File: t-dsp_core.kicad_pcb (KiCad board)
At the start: 4 copper layers, 100 x 61 mm, 164 parts, among them IC1 Logic Level Shifter - 74HCT2G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, J1 J_PWR, J10 J_DMX, J11 J_LED, J12 J_ETH, J13 u.FL DNP (IDC767 ext-antenna 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, J2 J_TDM, J3 J_T, J4 J_USBH, J5 J_MIDI, J6 J_SPDIF, J7 J_AUX, J8 J_S3, T108 Tab, T109 Tab, T110 Tab, T111 Tab, U1 Teensy 4.1 - DEVKIT, U11 Dual Buffer - SN74LVC2G125DCTR, U13 ESP32-S3-WROOM-1-N16R8, U15 LT3045EMSE#TRPBF, U16 THVD1450DR, U17 ISO7762DW, U18 TEA1-0505HI, U19 SRC4382IPFBR, U20 TLV75718PDRVR, U21 74LVC157APW, U22 IDC777-1, U23 74LVC157APW, U24 AP63203WU, U3 Power Mux & Protect - TPS2116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, U4 Optoisolators - H11L1SM - 6-S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, U5 Dual Buffer - SN74LVC2G125DCTR, U6 Dual Buffer - SN74LVC2G125DCTR, U7 Dual Buffer - SN74LVC2G125DCTR, U8 Dual Buffer - SN74LVC2G125DCTR, U9 Dual Buffer - 74HCT2G17GW,125, Y1 24.576MHz

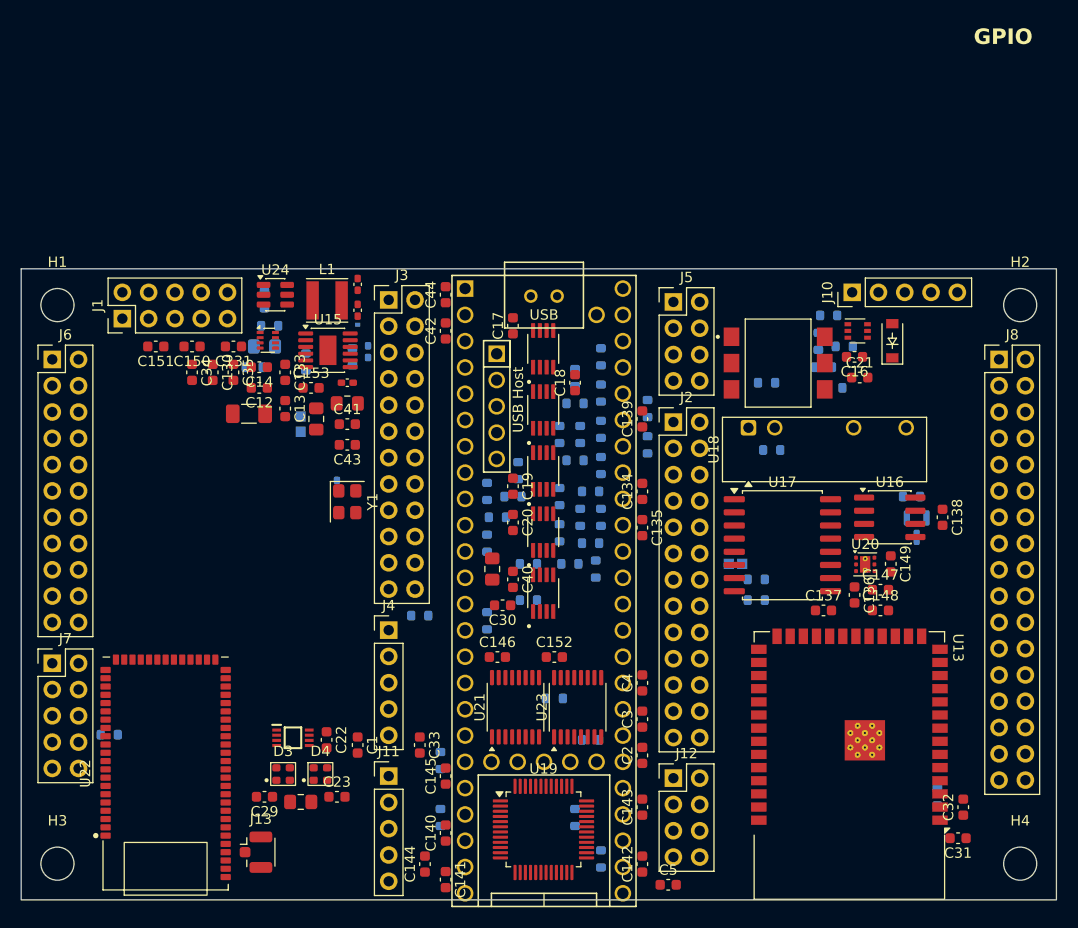
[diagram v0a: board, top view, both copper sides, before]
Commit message: Spin 2 stage 10r (board): U5 -> TSSOP-20 octal buffer at the top of the column under the Teensy, U6-U8 and C18-C20 removed, JP1 and R74 added on the back; pad nets, values and fields synced from the schematic with pcbnew; passives re-placed
Co-Authored-By: Claude Fable 5.1 <noreply@anthropic.com>
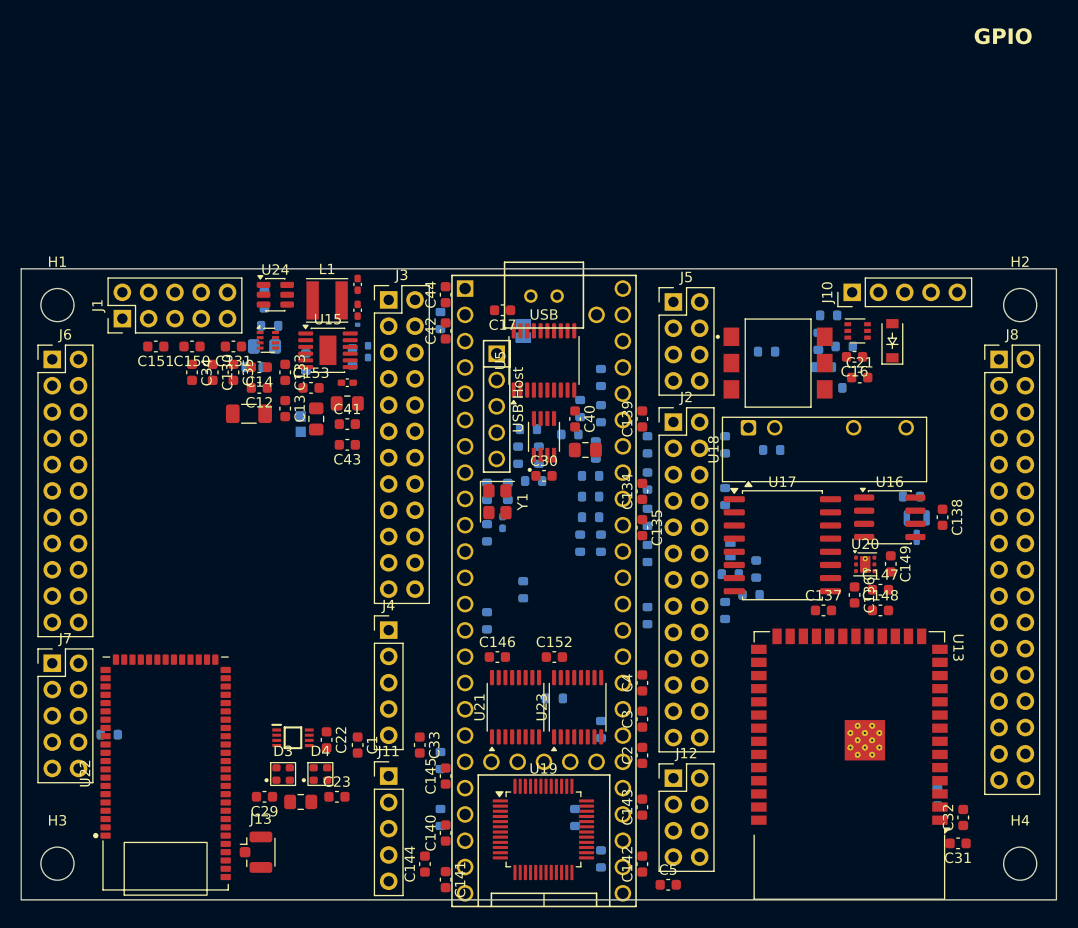
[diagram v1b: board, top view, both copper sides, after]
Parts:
- removed C18, C19, C20: 0.1 uF, Capacitor_SMD:C_0603_1608Metric
- removed U6, U7, U8: Dual Buffer - SN74LVC2G125DCTR, project_fp:SOP65P400X130-8N
- added JP1: SJ bridged, Jumper:SolderJumper-2_P1.3mm_Bridged_Pad1.0x1.5mm, B.Cu at (148.5, 145.0)
- added R74: 10k, Resistor_SMD:R_0603_1608Metric, B.Cu at (140.5, 144.0)
- U5: value Dual Buffer - SN74LVC2G125DCTR -> SN74LVC541APWR; footprint project_fp:SOP65P400X130-8N -> Package_SO:TSSOP-20_4.4x6.5mm_P0.65mm
- moved R43 21.5 mm to (168.5, 168.5), turned to 180 degrees
- moved R42 18.4 mm to (160.5, 166.5), turned to 90 degrees
- moved C40 16.6 mm to (153.5, 153.5)
- moved R60 16.4 mm to (146.5, 163.5), turned to -90 degrees
- moved R45 16.0 mm to (168.0, 161.0)
- moved U11 15.1 mm to (150.5, 155.3)
- moved C27 14.6 mm to (154.5, 156.5), turned to 0 degrees
- moved Y1 14.5 mm to (146.0, 161.5)
- moved R40 14.0 mm to (168.0, 156.0)
- moved C30 13.1 mm to (150.5, 159.0), turned to 0 degrees
- moved R47 13.1 mm to (168.0, 172.0), turned to 90 degrees
- moved R56 11.5 mm to (149.5, 159.5)
- moved R55 10.5 mm to (150.0, 157.0), turned to -90 degrees
- moved R61 10.3 mm to (148.5, 170.0), turned to -90 degrees
- moved R41 10.3 mm to (160.5, 159.5), turned to 90 degrees
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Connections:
- R40 pad 1: Net-(U6-2Y) -> /TDM2_MCLK_B
- R41 pad 1: Net-(U6-1Y) -> /TDM1_MCLK_B
- R42 pad 1: Net-(U5-1Y) -> /TDM1_LRCK_B
- R43 pad 1: Net-(U5-2Y) -> /TDM2_LRCK_B
- R44 pad 1: Net-(U7-1Y) -> /TDM1_BCLK_B
- R45 pad 1: Net-(U7-2Y) -> /TDM2_BCLK_B
- R46 pad 1: Net-(U8-1Y) -> /TDM1_DOUT_B
- R47 pad 1: Net-(U8-2Y) -> /TDM2_DOUT_B
- U5 pad 3: Net-(U5-2Y) -> MCLK1
- U5 pad 4: GND -> BCLK1
- U5 pad 5: LRCK1 -> 7_OUT1A
- U5 pad 6: Net-(U5-1Y) -> LRCK1
- U5 pad 7: GND -> MCLK1
- U5 pad 8: 3.3V -> BCLK1

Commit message: Spin 2 stage 10s: S3 and IDC777 swapped (S3 bottom-left with J8 on the left edge, IDC777 bottom-right with J6/J7 on the right edge), chips spread with 2-3 mm air, passive spacing margin 0.35 mm; change map 11.6
Co-Authored-By: Claude Fable 5.1 <noreply@anthropic.com>
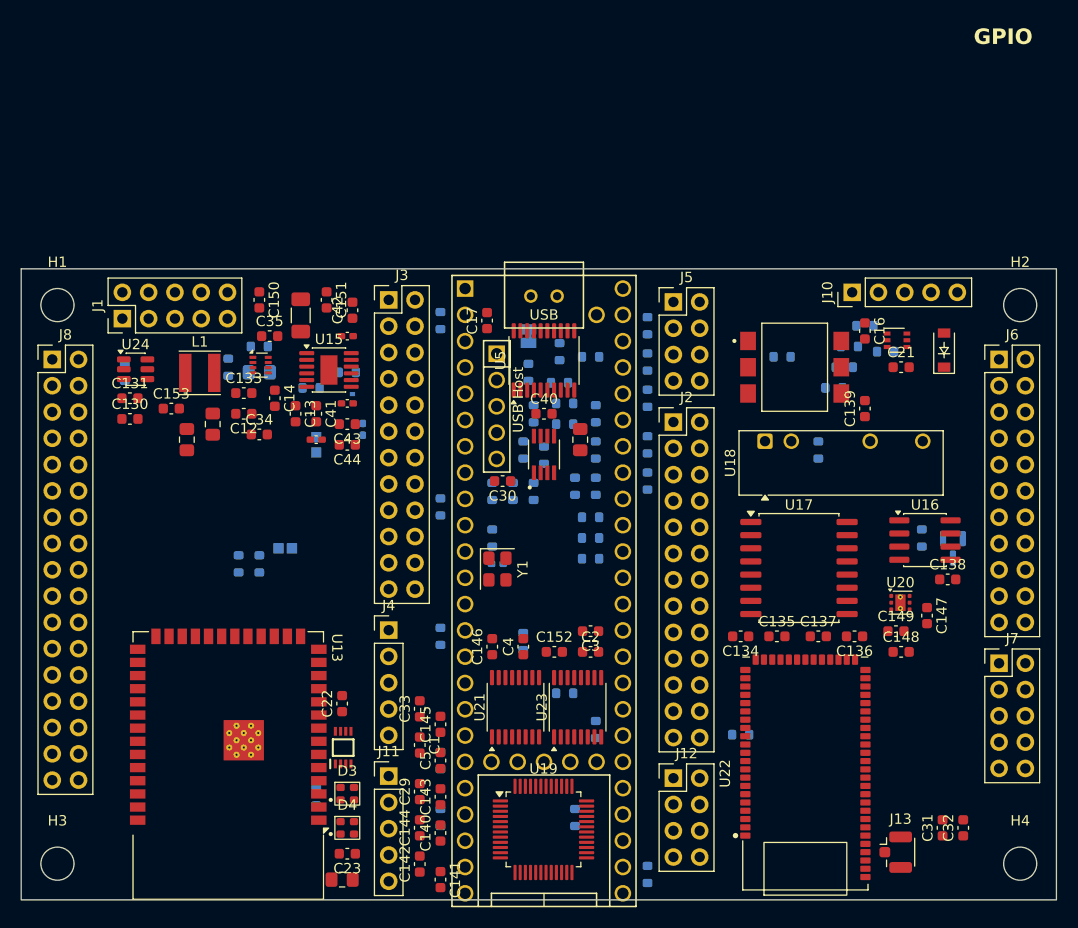
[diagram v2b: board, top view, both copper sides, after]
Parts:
- moved J6 91.5 mm to (194.5, 147.8)
- moved J7 91.5 mm to (194.5, 177.1)
- moved J8 91.5 mm to (103.0, 147.8)
- moved U22 61.8 mm to (175.8, 187.8)
- moved J13 61.8 mm to (184.9, 195.4)
- moved R72 61.0 mm to (169.5, 184.0), turned to 180 degrees
- moved R73 60.0 mm to (128.5, 190.0)
- moved U13 60.0 mm to (120.0, 187.0)
- moved R68 49.6 mm to (121.0, 167.5), turned to -90 degrees
- moved R67 48.0 mm to (123.0, 167.5)
- moved PU_EN1 43.0 mm to (125.5, 166.0), turned to 180 degrees
- moved C5 25.1 mm to (140.5, 186.5), turned to 90 degrees
- moved R43 23.0 mm to (152.5, 152.0), turned to 0 degrees
- moved R47 21.8 mm to (160.5, 151.5), turned to -90 degrees
- moved C139 21.5 mm to (181.5, 152.5)
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
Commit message: Spin 2 stage 10t: IDC777 5.4 mm further right (45.6 mm from the S3), J8 lowered beside the S3, J4 USB host header beside the Teensy host pads; passives re-placed
Co-Authored-By: Claude Fable 5.1 <noreply@anthropic.com>
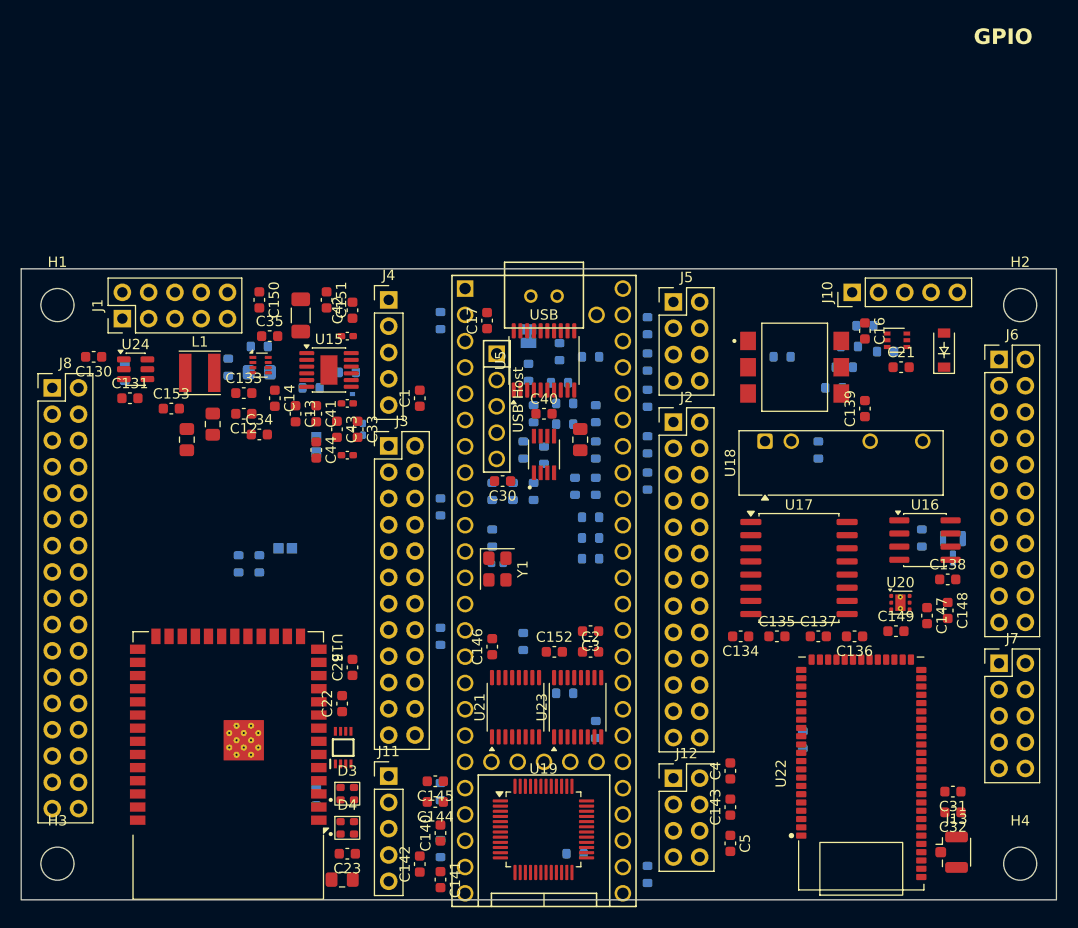
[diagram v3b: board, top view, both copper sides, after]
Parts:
- moved C1 33.5 mm to (138.5, 151.5), turned to 90 degrees
- moved J4 31.9 mm to (135.5, 142.0)
- moved C5 29.1 mm to (168.5, 194.5), turned to -90 degrees
- moved C143 28.0 mm to (168.5, 191.0)
- moved C33 27.7 mm to (132.5, 154.5), turned to -90 degrees
- moved C4 23.3 mm to (168.5, 187.5)
- moved J3 14.1 mm to (135.5, 156.1)
- moved C29 13.6 mm to (132.0, 177.5)
- moved C130 6.95 mm to (107.0, 147.5), turned to 180 degrees
- moved C148 6.02 mm to (189.5, 172.0), turned to -90 degrees
- moved R72 6.02 mm to (175.5, 184.5), turned to -90 degrees
- moved C145 5.52 mm to (140.0, 188.5), turned to 180 degrees
- moved J13 5.40 mm to (190.3, 195.4)
- moved U22 5.40 mm to (181.2, 187.8)
- moved C31 3.64 mm to (190.0, 189.5), turned to 180 degrees
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
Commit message: Spin 2 stage 10u (board): 20 terminations on 0402 footprints, values/fields/nets synced with pcbnew, passives re-placed
Co-Authored-By: Claude Fable 5.1 <noreply@anthropic.com>
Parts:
- R1, R10, R2, R3, R4, R40, R41, R42, R43, R44, R45, R46, R47, R5, R52, R55, R56, R6, R7, R9: value 49.9 ohm -> 33 ohm
- moved C31 0.50 mm to (190.5, 189.5)
- moved C32 0.50 mm to (190.5, 191.5)
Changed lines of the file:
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@@
 	(footprint "Capacitor_SMD:C_0603_1608Metric"
 		(layer "F.Cu")
-		(at 190 189.54 180)
+		(at 190.5 189.54 180)
 		(descr "Capacitor SMD 0603 (1608 Metric), square (rectangular) end terminal, IPC-7351 nominal, (Body size source: IPC-SM-782 page 76, https://www.pcb-3d.com/wordpress/wp-content/uploads/ipc-sm-782a_amendment_1_and_2.pdf)")
 		(tags "capacitor")
@@
 	(footprint "Capacitor_SMD:C_0603_1608Metric"
 		(layer "F.Cu")
-		(at 190 191.54 180)
+		(at 190.5 191.54 180)
 		(descr "Capacitor SMD 0603 (1608 Metric), square (rectangular) end terminal, IPC-7351 nominal, (Body size source: IPC-SM-782 page 76, https://www.pcb-3d.com/wordpress/wp-content/uploads/ipc-sm-782a_amendment_1_and_2.pdf)")
 		(tags "capacitor")
@@
 			)
 		)
-		(property "Value" "49.9 ohm"
+		(property "Value" "33 ohm"
 			(at 0 -1.43 90)
 			(layer "B.Fab")
@@
 			)
 		)
-		(property "LCSC" "C23185"
+		(property "LCSC" "C25105"
 			(at 0 0 0)
 			(layer "B.SilkS")
@@
 			)
 		)
-		(property "LCSC_MPN" "0603WAF499JT5E"
+		(property "LCSC_MPN" "0402WGF330JTCE"
 			(at 0 0 0)
 			(layer "B.SilkS")
@@
 			)
 		)
-		(property "Value" "49.9 ohm"
+		(property "Value" "33 ohm"
 			(at 0 -1.43 180)
 			(layer "B.Fab")
@@
 			)
 		)
-		(property "LCSC" "C23185"
+		(property "LCSC" "C25105"
 			(at 0 0 0)
 			(layer "B.SilkS")
@@
 			)
 		)
-		(property "LCSC_MPN" "0603WAF499JT5E"
+		(property "LCSC_MPN" "0402WGF330JTCE"
 			(at 0 0 0)
 			(layer "B.SilkS")
@@
 			)
 		)
-		(property "Value" "49.9 ohm"
+		(property "Value" "33 ohm"
 			(at 0 -1.43 90)
 			(layer "B.Fab")
@@
 			)
 		)
-		(property "LCSC" "C23185"
+		(property "LCSC" "C25105"
 			(at 0 0 270)
 			(layer "B.SilkS")
@@
 			)
 		)
-		(property "LCSC_MPN" "0603WAF499JT5E"
+		(property "LCSC_MPN" "0402WGF330JTCE"
 			(at 0 0 270)
 			(layer "B.SilkS")
@@
 			)
 		)
-		(property "Value" "49.9 ohm"
+		(property "Value" "33 ohm"
 			(at 0 -1.43 90)
 			(layer "B.Fab")
@@
 			)
 		)
-		(property "LCSC" "C23185"
+		(property "LCSC" "C25105"
 			(at 0 0 180)
 			(layer "B.SilkS")
@@
 			)
 		)
-		(property "LCSC_MPN" "0603WAF499JT5E"
+		(property "LCSC_MPN" "0402WGF330JTCE"
 			(at 0 0 180)
 			(layer "B.SilkS")
@@
 			)
 		)
-		(property "Value" "49.9 ohm"
+		(property "Value" "33 ohm"
 			(at 0 -1.43 270)
 			(layer "B.Fab")
@@
 			)
 		)
-		(property "LCSC" "C23185"
+		(property "LCSC" "C25105"
 			(at 0 0 270)
 			(layer "B.SilkS")
@@
 			)
 		)
-		(property "LCSC_MPN" "0603WAF499JT5E"
+		(property "LCSC_MPN" "0402WGF330JTCE"
 			(at 0 0 270)
 			(layer "B.SilkS")
@@
 			)
 		)
-		(property "Value" "49.9 ohm"
+		(property "Value" "33 ohm"
 			(at 0 -1.43 180)
 			(layer "B.Fab")
@@
 			)
 		)
-		(property "LCSC" "C23185"
+		(property "LCSC" "C25105"
 			(at 0 0 270)
 			(layer "B.SilkS")
@@
 			)
 		)
-		(property "LCSC_MPN" "0603WAF499JT5E"
+		(property "LCSC_MPN" "0402WGF330JTCE"
 			(at 0 0 270)
 			(layer "B.SilkS")
@@
 			)
 		)
-		(property "Value" "49.9 ohm"
+		(property "Value" "33 ohm"
 			(at 0 -1.43 90)
 			(layer "B.Fab")
@@
 			)
 		)
-		(property "LCSC" "C23185"
+		(property "LCSC" "C25105"
 			(at 0 0 90)
 			(layer "B.SilkS")
@@
 			)
 		)
-		(property "LCSC_MPN" "0603WAF499JT5E"
+		(property "LCSC_MPN" "0402WGF330JTCE"
 			(at 0 0 90)
 			(layer "B.SilkS")
@@
 			)
 		)
-		(property "Value" "49.9 ohm"
+		(property "Value" "33 ohm"
 			(at 0 -1.43 270)
 			(layer "B.Fab")
@@
 			)
 		)
-		(property "LCSC" "C23185"
+		(property "LCSC" "C25105"
 			(at 0 0 90)
 			(layer "B.SilkS")
@@
 			)
 		)
-		(property "LCSC_MPN" "0603WAF499JT5E"
+		(property "LCSC_MPN" "0402WGF330JTCE"
 			(at 0 0 90)
 			(layer "B.SilkS")
@@
 			)
 		)
-		(property "Value" "49.9 ohm"
+		(property "Value" "33 ohm"
 			(at 0 -1.43 90)
 			(layer "B.Fab")
@@
 			)
 		)
-		(property "LCSC" "C23185"
+		(property "LCSC" "C25105"
 			(at 0 0 90)
 			(layer "B.SilkS")
@@
 			)
 		)
-		(property "LCSC_MPN" "0603WAF499JT5E"
+		(property "LCSC_MPN" "0402WGF330JTCE"
 			(at 0 0 90)
 			(layer "B.SilkS")
@@
 			)
 		)
-		(property "Value" "49.9 ohm"
+		(property "Value" "33 ohm"
 			(at 0 -1.43 180)
 			(layer "B.Fab")
@@
 			)
 		)
-		(property "LCSC" "C23185"
+		(property "LCSC" "C25105"
 			(at 0 0 0)
 			(layer "B.SilkS")
@@
 			)
 		)
-		(property "LCSC_MPN" "0603WAF499JT5E"
+		(property "LCSC_MPN" "0402WGF330JTCE"
 			(at 0 0 0)
 			(layer "B.SilkS")
@@
 			)
 		)
-		(property "Value" "49.9 ohm"
+		(property "Value" "33 ohm"
 			(at 0 -1.43 90)
 			(layer "B.Fab")
@@
 			)
 		)
-		(property "LCSC" "C23185"
+		(property "LCSC" "C25105"
 			(at 0 0 180)
 			(layer "B.SilkS")
@@
 			)
 		)
-		(property "LCSC_MPN" "0603WAF499JT5E"
+		(property "LCSC_MPN" "0402WGF330JTCE"
 			(at 0 0 180)
 			(layer "B.SilkS")
@@
 			)
 		)
-		(property "Value" "49.9 ohm"
+		(property "Value" "33 ohm"
 			(at 0 -1.43 270)
 			(layer "B.Fab")
@@
 			)
 		)
-		(property "LCSC" "C23185"
+		(property "LCSC" "C25105"
 			(at 0 0 0)
 			(layer "B.SilkS")
@@
 			)
 		)
-		(property "LCSC_MPN" "0603WAF499JT5E"
+		(property "LCSC_MPN" "0402WGF330JTCE"
 			(at 0 0 0)
 			(layer "B.SilkS")
@@
 			)
 		)
-		(property "Value" "49.9 ohm"
+		(property "Value" "33 ohm"
 			(at 0 -1.43 270)
 			(layer "B.Fab")
@@
 			)
 		)
-		(property "LCSC" "C23185"
+		(property "LCSC" "C25105"
 			(at 0 0 180)
 			(layer "B.SilkS")
@@
 			)
 		)
-		(property "LCSC_MPN" "0603WAF499JT5E"
+		(property "LCSC_MPN" "0402WGF330JTCE"
 			(at 0 0 180)
 			(layer "B.SilkS")
@@
 			)
 		)
-		(property "Value" "49.9 ohm"
+		(property "Value" "33 ohm"
 			(at 0 -1.43 90)
 			(layer "B.Fab")
@@
 			)
 		)
-		(property "LCSC" "C23185"
+		(property "LCSC" "C25105"
 			(at 0 0 270)
 			(layer "B.SilkS")
@@
 			)
 		)
-		(property "LCSC_MPN" "0603WAF499JT5E"
+		(property "LCSC_MPN" "0402WGF330JTCE"
 			(at 0 0 270)
 			(layer "B.SilkS")
@@
 			)
 		)
-		(property "Value" "49.9 ohm"
+		(property "Value" "33 ohm"
 			(at 0 -1.43 90)
 			(layer "B.Fab")
@@
 			)
 		)
-		(property "LCSC" "C23185"
+		(property "LCSC" "C25105"
 			(at 0 0 180)
 			(layer "B.SilkS")
@@
 			)
 		)
-		(property "LCSC_MPN" "0603WAF499JT5E"
+		(property "LCSC_MPN" "0402WGF330JTCE"
 			(at 0 0 180)
 			(layer "B.SilkS")
@@
 			)
 		)
-		(property "Value" "49.9 ohm"
+		(property "Value" "33 ohm"
 			(at 0 -1.43 270)
 			(layer "B.Fab")
@@
 			)
 		)
-		(property "LCSC" "C23185"
+		(property "LCSC" "C25105"
 			(at 0 0 0)
 			(layer "B.SilkS")
@@
 			)
 		)
-		(property "LCSC_MPN" "0603WAF499JT5E"
+		(property "LCSC_MPN" "0402WGF330JTCE"
 			(at 0 0 0)
 			(layer "B.SilkS")
@@
 			)
 		)
-		(property "Value" "49.9 ohm"
+		(property "Value" "33 ohm"
 			(at 0 -1.43 0)
 			(layer "B.Fab")
@@
 			)
 		)
-		(property "LCSC" "C23185"
+		(property "LCSC" "C25105"
 			(at 0 0 90)
 			(layer "B.SilkS")
@@
 			)
 		)
-		(property "LCSC_MPN" "0603WAF499JT5E"
+		(property "LCSC_MPN" "0402WGF330JTCE"
 			(at 0 0 90)
 			(layer "B.SilkS")
@@
 			)
 		)
-		(property "Value" "49.9 ohm"
+		(property "Value" "33 ohm"
 			(at 0 -1.43 270)
 			(layer "B.Fab")
@@
 			)
 		)
-		(property "LCSC" "C23185"
+		(property "LCSC" "C25105"
 			(at 0 0 180)
 			(layer "B.SilkS")
@@
 			)
 		)
-		(property "LCSC_MPN" "0603WAF499JT5E"
+		(property "LCSC_MPN" "0402WGF330JTCE"
 			(at 0 0 180)
 			(layer "B.SilkS")
@@
 			)
 		)
-		(property "Value" "49.9 ohm"
+		(property "Value" "33 ohm"
 			(at 0 -1.43 90)
 			(layer "B.Fab")
@@
 			)
 		)
-		(property "LCSC" "C23185"
+		(property "LCSC" "C25105"
 			(at 0 0 180)
 			(layer "B.SilkS")
@@
 			)
 		)
-		(property "LCSC_MPN" "0603WAF499JT5E"
+		(property "LCSC_MPN" "0402WGF330JTCE"
 			(at 0 0 180)
 			(layer "B.SilkS")
@@
 			)
 		)
-		(property "Value" "49.9 ohm"
+		(property "Value" "33 ohm"
 			(at 0 -1.43 180)
 			(layer "B.Fab")
@@
 			)
 		)
-		(property "LCSC" "C23185"
+		(property "LCSC" "C25105"
 			(at 0 0 0)
 			(layer "B.SilkS")
@@
 			)
 		)
-		(property "LCSC_MPN" "0603WAF499JT5E"
+		(property "LCSC_MPN" "0402WGF330JTCE"
 			(at 0 0 0)
 			(layer "B.SilkS")

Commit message: Spin 2 stage 10u (board, fix): terminations really on 0402 footprints now (footprint sync reloads the board between phases); passives re-placed; change map note
Co-Authored-By: Claude Fable 5.1 <noreply@anthropic.com>
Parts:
- R1, R10, R2, R3, R4, R40, R41, R42, R43, R44, R45, R46, R47, R5, R52, R55, R56, R6, R7, R9: footprint Resistor_SMD:R_0603_1608Metric -> Resistor_SMD:R_0402_1005Metric
- moved R9 8.50 mm to (153.0, 155.5), turned to 180 degrees
- moved R7 5.22 mm to (155.5, 146.0), turned to 180 degrees
- moved R2 5.00 mm to (145.5, 162.0), turned to 0 degrees
- moved R45 4.74 mm to (156.0, 149.5)
- moved R44 4.61 mm to (152.5, 146.0), turned to 0 degrees
- moved R6 3.64 mm to (153.0, 154.0), turned to 180 degrees
- moved R43 2.83 mm to (154.5, 150.0), turned to -90 degrees
- moved R46 2.00 mm to (152.5, 152.0), turned to -90 degrees
- moved R47 1.50 mm to (160.5, 150.0)
- moved R3 1.12 mm to (146.5, 160.0)
- moved R55 1.12 mm to (149.5, 156.5)
- moved R1 0.71 mm to (145.0, 160.0)
- moved R4 0.71 mm to (148.0, 157.0)
- moved R41 0.71 mm to (152.5, 147.5), turned to 0 degrees
- moved R56 0.71 mm to (149.0, 160.0), turned to 180 degrees
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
